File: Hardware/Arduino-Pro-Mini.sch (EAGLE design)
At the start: 28 parts, among them Q1 8/16/20MHz, U1 ATMEGA328, U2 MIC5205

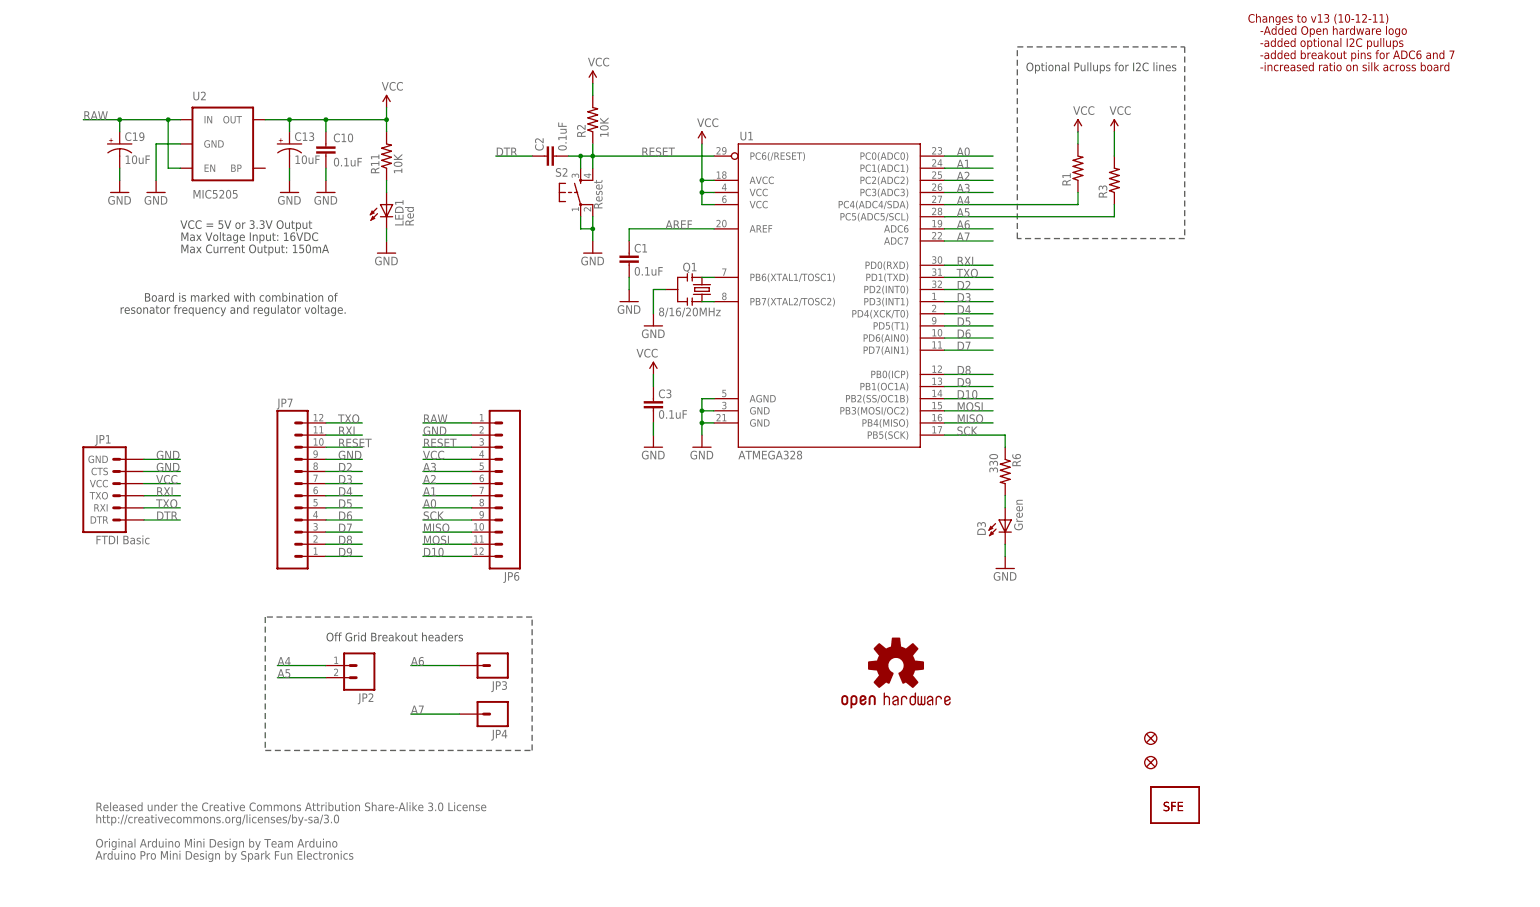
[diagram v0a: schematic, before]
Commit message: updated frame in SCH
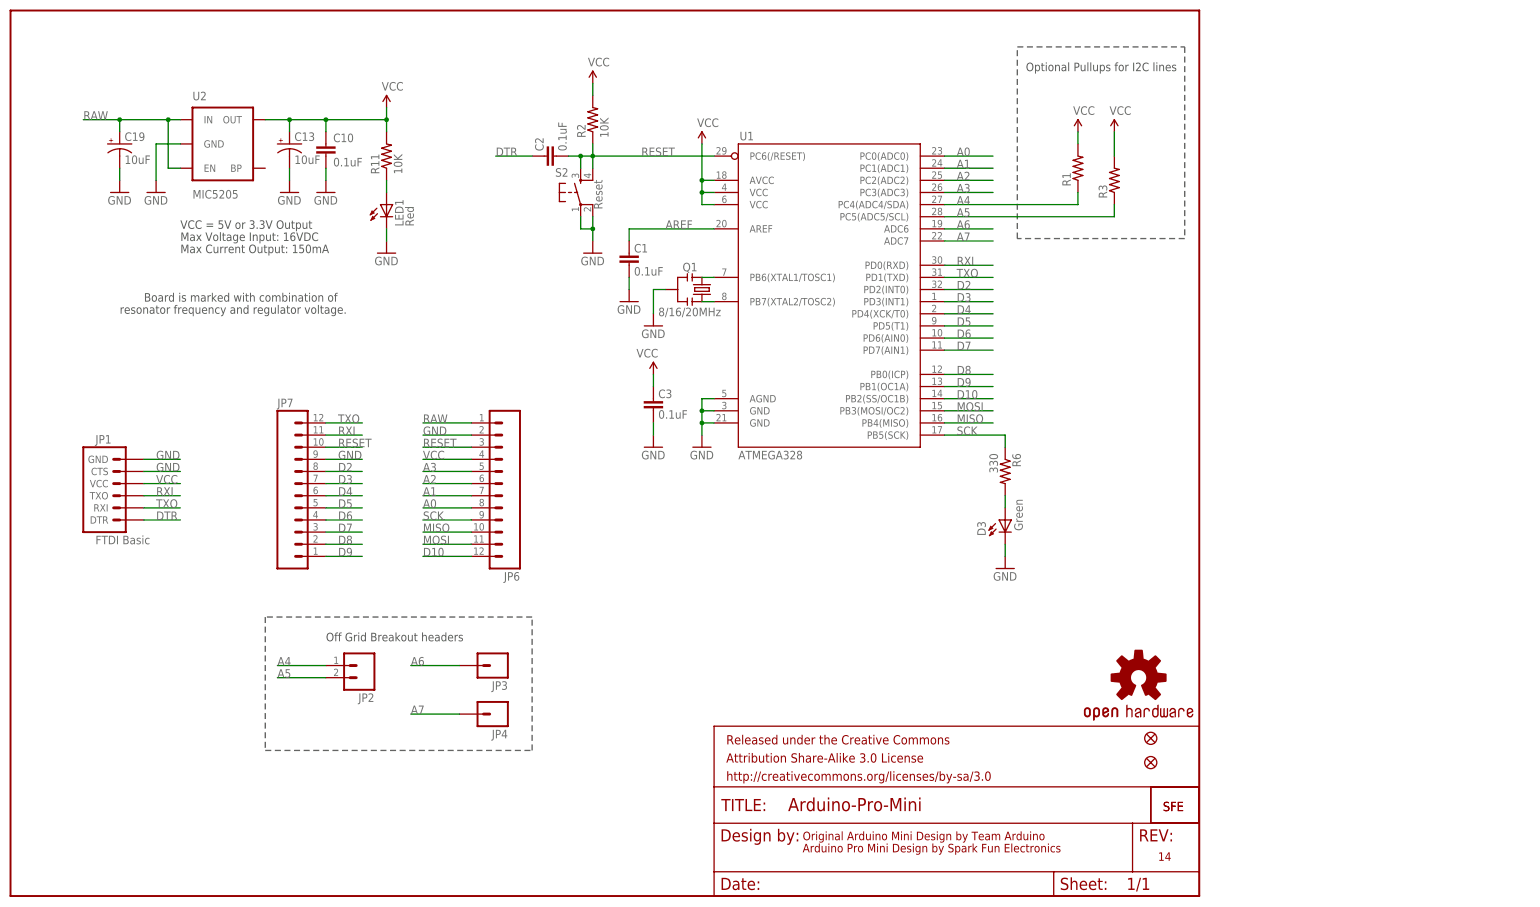
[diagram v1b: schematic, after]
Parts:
- added FRAME1: FRAME-LETTER, SparkFun-Aesthetics:FRAME-LETTER
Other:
- note added: "14"
- note removed: "-Added Open hardware logo"
- note removed: "-added breakout pins for ADC6 and 7"
- note removed: "-added optional I2C pullups"
- note removed: "-increased ratio on silk across board"
- note removed: "Changes to v13 (10-12-11)"
- note removed: "Released under the Creative Commons Attribution Share-Alike 3.0 License"
- note removed: "http://creativecommons.org/licenses/by-sa/3.0"
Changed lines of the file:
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@@
 <layer number="144" name="Drill_legend" color="7" fill="1" visible="yes" active="yes"/>
 <layer number="151" name="HeatSink" color="7" fill="1" visible="yes" active="yes"/>
+<layer number="199" name="Contour" color="7" fill="1" visible="yes" active="yes"/>
 <layer number="200" name="200bmp" color="1" fill="10" visible="no" active="no"/>
 <layer number="201" name="201bmp" color="2" fill="1" visible="no" active="no"/>
@@
 <parts>
 <part name="C10" library="SparkFun" deviceset="CAP" device="0603-CAP" value="0.1uF"/>
-<part name="FRAME1" library="SparkFun" deviceset="FRAME-LETTER" device=""/>
+<part name="FRAME1" library="SparkFun-Aesthetics" deviceset="FRAME-LETTER" device=""/>
 <part name="C13" library="SparkFun" deviceset="CAP_POL" device="1206" value="10uF"/>
 <part name="GND25" library="SparkFun" deviceset="GND" device=""/>
@@
 <wire x1="53.34" y1="30.48" x2="109.22" y2="30.48" width="0.2032" layer="97" style="shortdash"/>
 <wire x1="109.22" y1="30.48" x2="109.22" y2="58.42" width="0.2032" layer="97" style="shortdash"/>
-<text x="17.78" y="17.78" size="1.778" layer="95">Released under the Creative Commons Attribution Share-Alike 3.0 License</text>
-<text x="17.78" y="15.24" size="1.778" layer="95">http://creativecommons.org/licenses/by-sa/3.0</text>
-<text x="17.78" y="10.16" size="1.778" layer="95">Original Arduino Mini Design by Team Arduino</text>
-<text x="17.78" y="7.62" size="1.778" layer="95">Arduino Pro Mini Design by Spark Fun Electronics</text>
+<text x="165.862" y="11.684" size="1.778" layer="94">Original Arduino Mini Design by Team Arduino</text>
+<text x="165.862" y="9.144" size="1.778" layer="94">Arduino Pro Mini Design by Spark Fun Electronics</text>
 <text x="35.56" y="137.16" size="1.778" layer="97">Max Voltage Input: 16VDC</text>
 <text x="35.56" y="134.62" size="1.778" layer="97">Max Current Output: 150mA</text>
@@
 <text x="212.598" y="172.72" size="1.778" layer="97">Optional Pullups for I2C lines</text>
 <text x="66.04" y="53.34" size="1.778" layer="97">Off Grid Breakout headers</text>
-<text x="259.08" y="182.88" size="1.778" layer="94">Changes to v13 (10-12-11)</text>
-<text x="261.62" y="180.34" size="1.778" layer="94">-Added Open hardware logo</text>
-<text x="261.62" y="177.8" size="1.778" layer="94">-added optional I2C pullups</text>
-<text x="261.62" y="175.26" size="1.778" layer="94">-added breakout pins for ADC6 and 7</text>
-<text x="261.62" y="172.72" size="1.778" layer="94">-increased ratio on silk across board</text>
+<text x="240.284" y="7.366" size="1.778" layer="94">14</text>
 </plain>
 <instances>
@@
 <attribute name="VALUE" x="116.459" y="155.956" size="1.778" layer="96" rot="R90"/>
 </instance>
-<instance part="U$3" gate="G$1" x="185.42" y="48.26"/>
+<instance part="U$3" gate="G$1" x="236.22" y="45.72"/>
 <instance part="JP3" gate="G$1" x="101.6" y="48.26" rot="R180"/>
 <instance part="JP4" gate="G$1" x="101.6" y="38.1" rot="R180"/>

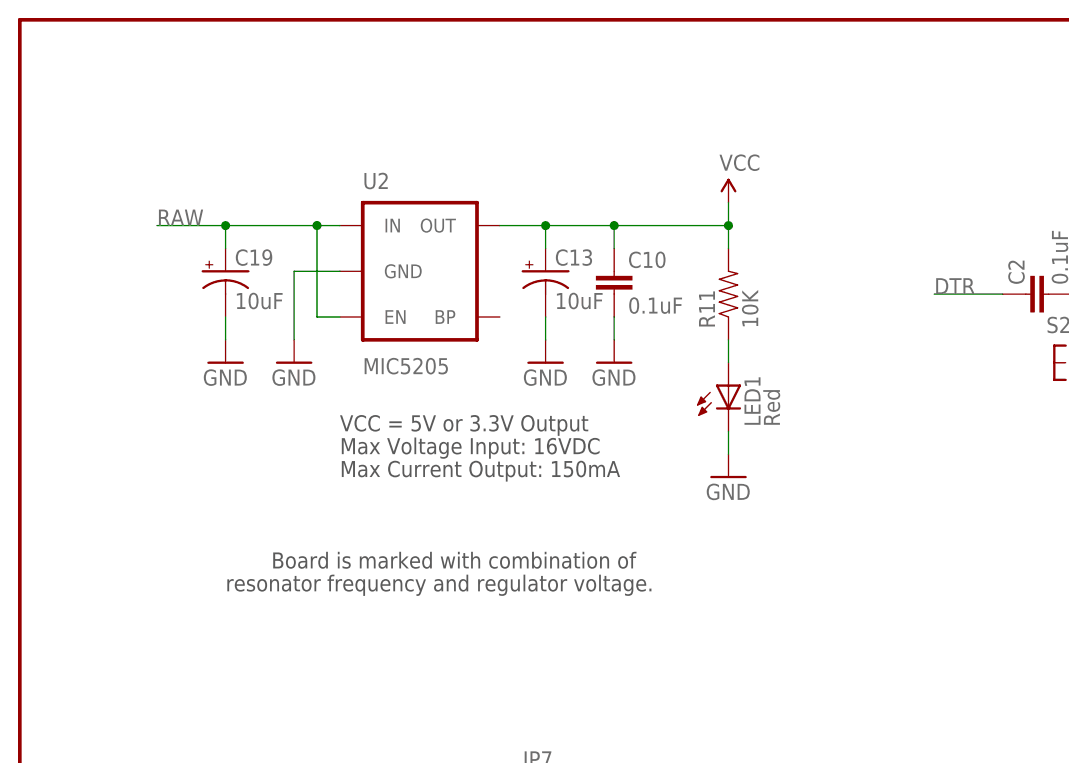
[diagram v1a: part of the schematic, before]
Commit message: Added power isolation jumper
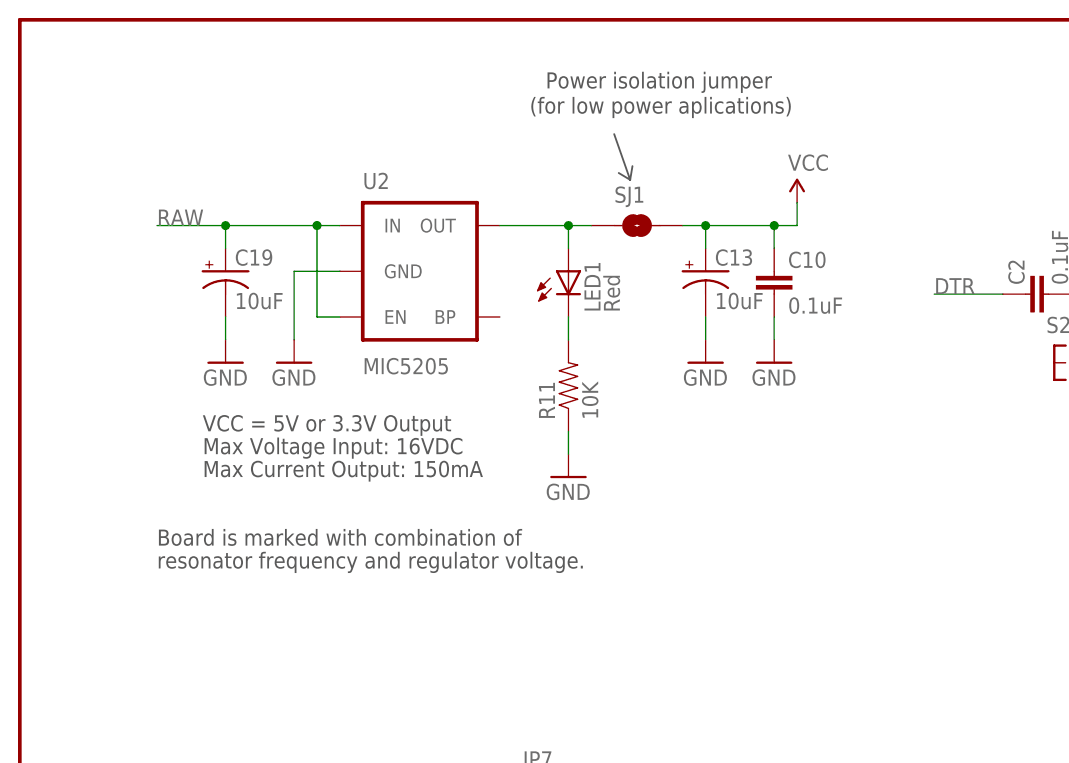
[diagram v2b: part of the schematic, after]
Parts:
- added SJ1: SOLDERJUMPERNC, SparkFun-Passives:SOLDERJUMPERNC
- R1, R3: device SparkFun:RESISTOR0402-RES -> SparkFun:RESISTOR0603-RES
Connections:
- removed net N$38: LED1.A, R11.1
- new net N$3: LED1.A, SJ1.1, U2.OUT
- new net N$4: LED1.C, R11.2
- net GND: now also R11.1; no longer LED1.C
- net VCC: now also SJ1.2; no longer R11.2, U2.OUT
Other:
- note added: "(for low power aplications)"
- note added: "Power isolation jumper"
- moved on the sheet: C10, C13, LED1, R11
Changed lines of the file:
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@@
 <layer number="106" name="bPlate" color="7" fill="1" visible="yes" active="yes"/>
 <layer number="107" name="Crop" color="7" fill="1" visible="yes" active="yes"/>
+<layer number="108" name="tplace-old" color="10" fill="1" visible="yes" active="yes"/>
+<layer number="109" name="ref-old" color="11" fill="1" visible="yes" active="yes"/>
 <layer number="116" name="Patch_BOT" color="9" fill="4" visible="yes" active="yes"/>
 <layer number="121" name="_tsilk" color="7" fill="1" visible="yes" active="yes"/>
@@
 <part name="GND32" library="SparkFun" deviceset="GND" device=""/>
 <part name="P+11" library="SparkFun" deviceset="3.3V" device="" value="VCC"/>
-<part name="P+12" library="SparkFun" deviceset="3.3V" device="" value="VCC"/>
 <part name="P+15" library="SparkFun" deviceset="3.3V" device="" value="VCC"/>
 <part name="JP6" library="SparkFun" deviceset="M12" device="PTH" value=""/>
@@
 <part name="JP3" library="SparkFun" deviceset="M01" device="PTH" value=""/>
 <part name="JP4" library="SparkFun" deviceset="M01" device="PTH" value=""/>
-<part name="R1" library="SparkFun" deviceset="RESISTOR" device="0402-RES"/>
-<part name="R3" library="SparkFun" deviceset="RESISTOR" device="0402-RES"/>
+<part name="R1" library="SparkFun" deviceset="RESISTOR" device="0603-RES"/>
+<part name="R3" library="SparkFun" deviceset="RESISTOR" device="0603-RES"/>
 <part name="P+2" library="SparkFun" deviceset="3.3V" device="" value="VCC"/>
 <part name="P+3" library="SparkFun" deviceset="3.3V" device="" value="VCC"/>
 <part name="JP5" library="SparkFun" deviceset="FIDUCIAL" device="UFIDUCIAL"/>
 <part name="JP8" library="SparkFun" deviceset="FIDUCIAL" device="UFIDUCIAL"/>
+<part name="SJ1" library="SparkFun-Passives" deviceset="SOLDERJUMPER" device="NC" value=""/>
+<part name="P+4" library="SparkFun" deviceset="3.3V" device="" value="VCC"/>
 </parts>
 <sheets>
@@
 <text x="165.862" y="11.684" size="1.778" layer="94">Original Arduino Mini Design by Team Arduino</text>
 <text x="165.862" y="9.144" size="1.778" layer="94">Arduino Pro Mini Design by Spark Fun Electronics</text>
-<text x="35.56" y="137.16" size="1.778" layer="97">Max Voltage Input: 16VDC</text>
-<text x="35.56" y="134.62" size="1.778" layer="97">Max Current Output: 150mA</text>
-<text x="27.94" y="124.46" size="1.778" layer="97">Board is marked with combination of</text>
-<text x="22.86" y="121.92" size="1.778" layer="97">resonator frequency and regulator voltage.</text>
-<text x="35.56" y="139.7" size="1.778" layer="97">VCC = 5V or 3.3V Output</text>
+<text x="20.32" y="137.16" size="1.778" layer="97">Max Voltage Input: 16VDC</text>
+<text x="20.32" y="134.62" size="1.778" layer="97">Max Current Output: 150mA</text>
+<text x="15.24" y="127" size="1.778" layer="97">Board is marked with combination of</text>
+<text x="15.24" y="124.46" size="1.778" layer="97">resonator frequency and regulator voltage.</text>
+<text x="20.32" y="139.7" size="1.778" layer="97">VCC = 5V or 3.3V Output</text>
 <text x="212.598" y="172.72" size="1.778" layer="97">Optional Pullups for I2C lines</text>
 <text x="66.04" y="53.34" size="1.778" layer="97">Off Grid Breakout headers</text>
 <text x="240.284" y="7.366" size="1.778" layer="94">14</text>
+<text x="58.42" y="177.8" size="1.778" layer="97">Power isolation jumper</text>
+<text x="56.642" y="175.006" size="1.778" layer="97">(for low power aplications)</text>
+<wire x1="66.04" y1="172.72" x2="67.818" y2="167.64" width="0.2032" layer="97"/>
+<wire x1="67.818" y1="167.64" x2="68.072" y2="169.164" width="0.2032" layer="97"/>
+<wire x1="67.818" y1="167.64" x2="66.548" y2="168.402" width="0.2032" layer="97"/>
 </plain>
 <instances>
-<instance part="C10" gate="G$1" x="66.04" y="154.94"/>
+<instance part="C10" gate="G$1" x="83.82" y="154.94"/>
 <instance part="FRAME1" gate="G$1" x="0" y="0"/>
 <instance part="FRAME1" gate="G$2" x="147.32" y="0"/>
-<instance part="C13" gate="G$1" x="58.42" y="157.48"/>
-<instance part="GND25" gate="1" x="58.42" y="147.32"/>
-<instance part="GND26" gate="1" x="66.04" y="147.32"/>
-<instance part="R11" gate="G$1" x="78.74" y="154.94" rot="R90"/>
-<instance part="LED1" gate="G$1" x="78.74" y="144.78"/>
-<instance part="GND28" gate="1" x="78.74" y="134.62"/>
+<instance part="C13" gate="G$1" x="76.2" y="157.48"/>
+<instance part="GND25" gate="1" x="76.2" y="147.32"/>
+<instance part="GND26" gate="1" x="83.82" y="147.32"/>
+<instance part="R11" gate="G$1" x="60.96" y="144.78" rot="R90"/>
+<instance part="LED1" gate="G$1" x="60.96" y="157.48"/>
+<instance part="GND28" gate="1" x="60.96" y="134.62"/>
 <instance part="R2" gate="G$1" x="121.92" y="162.56" rot="R90"/>
 <instance part="S2" gate="S" x="119.38" y="147.32" smashed="yes" rot="R90">
@@
 <instance part="GND32" gate="1" x="22.86" y="147.32"/>
 <instance part="P+11" gate="G$1" x="121.92" y="170.18"/>
-<instance part="P+12" gate="G$1" x="78.74" y="165.1"/>
 <instance part="P+15" gate="G$1" x="134.62" y="109.22" smashed="yes">
 <attribute name="VALUE" x="131.064" y="112.776" size="1.778" layer="96"/>
@@
 <instance part="JP5" gate="G$1" x="238.76" y="27.94"/>
 <instance part="JP8" gate="G$1" x="238.76" y="33.02"/>
+<instance part="SJ1" gate="1" x="68.58" y="162.56"/>
+<instance part="P+4" gate="G$1" x="86.36" y="165.1"/>
 </instances>
 <busses>
@@
 <net name="GND" class="1">
 <segment>
-<wire x1="58.42" y1="149.86" x2="58.42" y2="152.4" width="0.1524" layer="91"/>
+<wire x1="76.2" y1="149.86" x2="76.2" y2="152.4" width="0.1524" layer="91"/>
 <pinref part="C13" gate="G$1" pin="-"/>
 <pinref part="GND25" gate="1" pin="GND"/>
 </segment>
 <segment>
-<wire x1="66.04" y1="149.86" x2="66.04" y2="152.4" width="0.1524" layer="91"/>
+<wire x1="83.82" y1="149.86" x2="83.82" y2="152.4" width="0.1524" layer="91"/>
 <pinref part="C10" gate="G$1" pin="2"/>
 <pinref part="GND26" gate="1" pin="GND"/>
-</segment>
-<segment>
-<wire x1="78.74" y1="137.16" x2="78.74" y2="139.7" width="0.1524" layer="91"/>
-<pinref part="LED1" gate="G$1" pin="C"/>
-<pinref part="GND28" gate="1" pin="GND"/>
 </segment>
 <segment>
@@
 <label x="30.48" y="91.44" size="1.778" layer="95"/>
 <pinref part="JP1" gate="G$1" pin="GND"/>
+</segment>
+<segment>
+<pinref part="GND28" gate="1" pin="GND"/>
+<pinref part="R11" gate="G$1" pin="1"/>
+<wire x1="60.96" y1="139.7" x2="60.96" y2="137.16" width="0.1524" layer="91"/>
 </segment>
 </net>
@@
 </segment>
 </net>
-<net name="N$38" class="0">
-<segment>
-<wire x1="78.74" y1="147.32" x2="78.74" y2="149.86" width="0.1524" layer="91"/>
-<pinref part="R11" gate="G$1" pin="1"/>
-<pinref part="LED1" gate="G$1" pin="A"/>
-</segment>
-</net>
 <net name="MISO" class="0">
 <segment>
@@
 <label x="86.36" y="91.44" size="1.778" layer="95"/>
 <pinref part="JP6" gate="G$1" pin="4"/>
-</segment>
-<segment>
-<wire x1="53.34" y1="162.56" x2="58.42" y2="162.56" width="0.1524" layer="91"/>
-<wire x1="58.42" y1="162.56" x2="66.04" y2="162.56" width="0.1524" layer="91"/>
-<wire x1="66.04" y1="162.56" x2="78.74" y2="162.56" width="0.1524" layer="91"/>
-<wire x1="78.74" y1="162.56" x2="78.74" y2="165.1" width="0.1524" layer="91"/>
-<wire x1="78.74" y1="162.56" x2="78.74" y2="160.02" width="0.1524" layer="91"/>
-<wire x1="66.04" y1="162.56" x2="66.04" y2="160.02" width="0.1524" layer="91"/>
-<wire x1="58.42" y1="162.56" x2="58.42" y2="160.02" width="0.1524" layer="91"/>
-<junction x="78.74" y="162.56"/>
-<junction x="66.04" y="162.56"/>
-<junction x="58.42" y="162.56"/>
-<pinref part="U2" gate="G$1" pin="OUT"/>
-<pinref part="P+12" gate="G$1" pin="3.3V"/>
-<pinref part="R11" gate="G$1" pin="2"/>
-<pinref part="C10" gate="G$1" pin="1"/>
-<pinref part="C13" gate="G$1" pin="+"/>
 </segment>
 <segment>
@@
 <pinref part="R3" gate="G$1" pin="2"/>
 </segment>
+<segment>
+<pinref part="P+4" gate="G$1" pin="3.3V"/>
+<wire x1="86.36" y1="165.1" x2="86.36" y2="162.56" width="0.1524" layer="91"/>
+<pinref part="SJ1" gate="1" pin="2"/>
+<wire x1="86.36" y1="162.56" x2="83.82" y2="162.56" width="0.1524" layer="91"/>
+<pinref part="C13" gate="G$1" pin="+"/>
+<wire x1="83.82" y1="162.56" x2="76.2" y2="162.56" width="0.1524" layer="91"/>
+<wire x1="76.2" y1="162.56" x2="73.66" y2="162.56" width="0.1524" layer="91"/>
+<wire x1="76.2" y1="160.02" x2="76.2" y2="162.56" width="0.1524" layer="91"/>
+<junction x="76.2" y="162.56"/>
+<pinref part="C10" gate="G$1" pin="1"/>
+<wire x1="83.82" y1="160.02" x2="83.82" y2="162.56" width="0.1524" layer="91"/>
+<junction x="83.82" y="162.56"/>
+</segment>
 </net>
 <net name="RAW" class="1">
@@
 </segment>
 </net>
+<net name="N$3" class="0">
+<segment>
+<pinref part="U2" gate="G$1" pin="OUT"/>
+<wire x1="53.34" y1="162.56" x2="60.96" y2="162.56" width="0.1524" layer="91"/>
+<pinref part="SJ1" gate="1" pin="1"/>
+<pinref part="LED1" gate="G$1" pin="A"/>
+<wire x1="60.96" y1="162.56" x2="63.5" y2="162.56" width="0.1524" layer="91"/>
+<wire x1="60.96" y1="160.02" x2="60.96" y2="162.56" width="0.1524" layer="91"/>
+<junction x="60.96" y="162.56"/>
+</segment>
+</net>
+<net name="N$4" class="0">
+<segment>
+<pinref part="R11" gate="G$1" pin="2"/>
+<pinref part="LED1" gate="G$1" pin="C"/>
+<wire x1="60.96" y1="152.4" x2="60.96" y2="149.86" width="0.1524" layer="91"/>
+</segment>
+</net>
